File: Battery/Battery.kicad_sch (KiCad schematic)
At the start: 6 parts, among them J1 Conn_01x03_Pin, J2 Conn_01x05, J3 Conn_01x02, J4 Conn_01x04, J5 Conn_01x02, SW1 SW_SPST

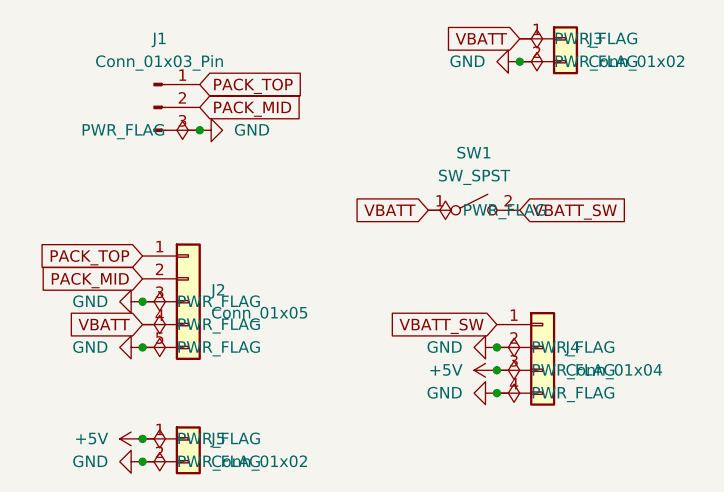
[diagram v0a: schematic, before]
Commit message: Battery Schematic and other stuff. Renaming main board files
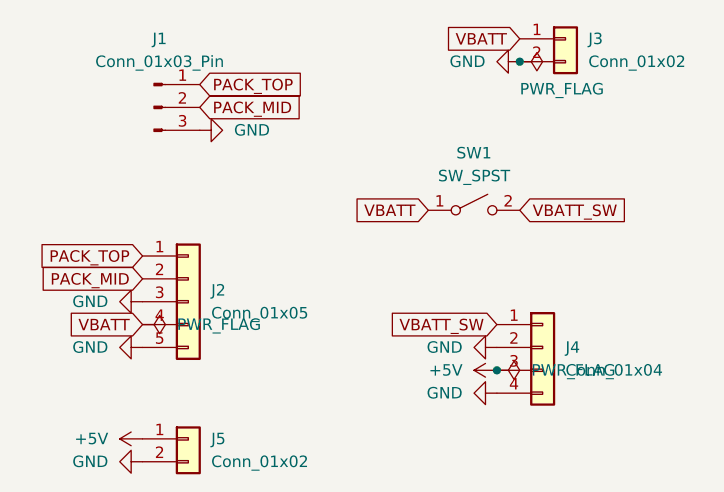
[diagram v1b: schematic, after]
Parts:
- J5: footprint (none) -> TerminalBlock_Phoenix:TerminalBlock_Phoenix_MKDS-1,5-2-5.08_1x02_P5.08mm_Horizontal
